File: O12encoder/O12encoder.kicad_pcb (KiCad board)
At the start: 2 copper layers, 14 x 14 mm, 15 parts, among them J1 Conn_01x06_Pin, J2 Conn_01x06_Pin, J3 Conn_01x06_Pin, J4 Conn_01x06_Pin, J5 SM02B-SRSS-TB_LF__SN_, J6 SM02B-SRSS-TB_LF__SN_, U1 QFN-3x3_MA702_MNP, U2 STM32L011F4Ux, U3 THVD1420DRLR

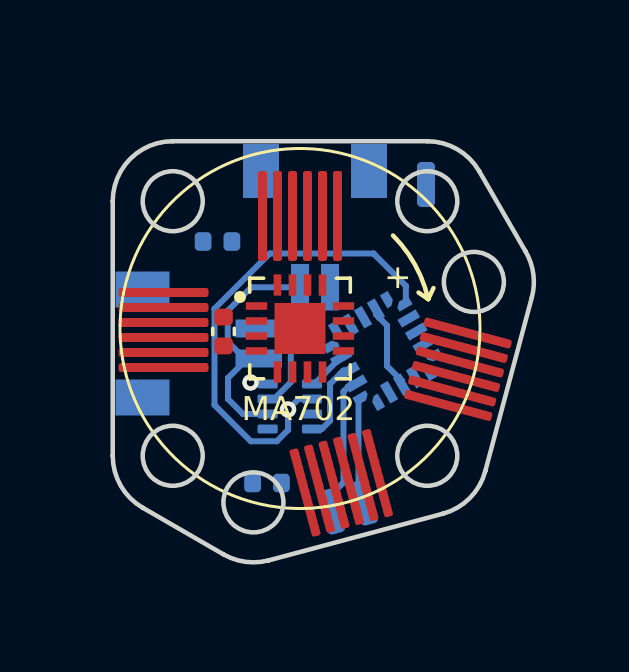
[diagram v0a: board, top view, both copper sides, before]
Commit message: encoder change to both sides FFC
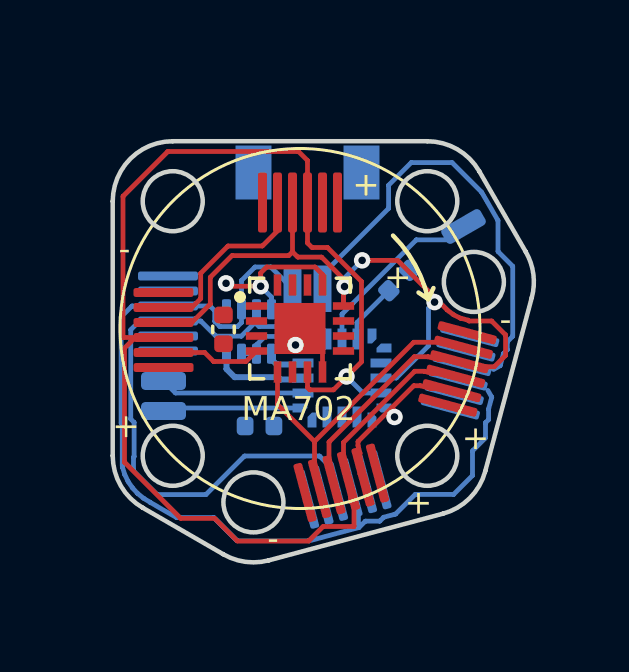
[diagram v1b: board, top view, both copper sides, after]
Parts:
- added J7: Conn_01x06_Pin, O32controller:FFC_0.5mm_6p, B.Cu at (55.7, 50.2)
- added J8: Conn_01x06_Pin, O32controller:FFC_0.5mm_6p, B.Cu at (50.3, 55.7)
- J5: value SM02B-SRSS-TB_LF__SN_ -> JST_SM02B-SRSS-TB(LF)(SN)
- J6: value SM02B-SRSS-TB_LF__SN_ -> Conn_01x06_Pin; footprint O32controller:JST_SM02B-SRSS-TB(LF)(SN) -> O32controller:FFC_0.5mm_6p
- U1: value QFN-3x3_MA702_MNP -> MA702GQ-P
- moved TP2 7.36 mm to (45.5, 52.8), turned to -90 degrees
- moved TP3 7.09 mm to (45.5, 51.8), turned to -90 degrees
- moved J6 6.39 mm to (45.6, 50.8)
- moved C3 6.19 mm to (53.3, 48.4), turned to 45 degrees
- moved J5 5.23 mm to (50.2, 46.7), turned to 0 degrees
- moved U3 2.85 mm to (48.3, 50.1), turned to 90 degrees
- moved J4 2.50 mm to (55.6, 50.1), turned to -15 degrees
- moved C2 1.92 mm to (48.6, 53.2)
- moved TP1 1.88 mm to (55.5, 46.6), turned to -60 degrees
- moved U2 1.62 mm to (51.4, 51.6), turned to -90 degrees
- moved J2 0.45 mm to (48.8, 45.8)
- moved C1 0.07 mm to (47.5, 50.0), turned to -90 degrees
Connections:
- net Net-(U2-NRST) renamed /NRST
- J6 pad 1: /RS485_A -> GND
- J6 pad 2: /RS485_B -> GND
- U1 pad 5: /~{MAG1_CS} -> /~{MAG2_CS}
- U2 pad 1: unconnected-(U2-PC14-Pad1) -> /UART_DE
- U2 pad 20: unconnected-(U2-PB9-Pad20) -> GND
- U2 pad 5: unconnected-(U2-PA0-Pad5) -> /ADC_IN0/WKUP
- U2 pad 6: /UART_DE -> unconnected-(U2-PA1-Pad6)
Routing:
- net /SPI_MISO: track 0.00 -> 46.0 mm, vias 0 -> 1
- net /SPI_SCLK: track 0.00 -> 29.2 mm, vias 0 -> 3
- net /RS485_B: track 7.08 -> 35.6 mm
- net /RS485_A: track 8.44 -> 30.8 mm
- net /~{MAG2_CS}: track 0.00 -> 15.3 mm
- net /UART_DE: track 16.0 -> 2.91 mm, vias 1 -> 0
- net /SPI_MOSI: track 0.00 -> 9.29 mm, vias 0 -> 1
- net /NRST: track 0.00 -> 6.04 mm
- net +3.3V: track 3.45 -> 7.15 mm, vias 1 -> 2
- net GND: track 0.00 -> 2.00 mm, vias 0 -> 1
- net /SWDIO: track 3.54 -> 4.52 mm
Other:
- board text added: "-"

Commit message: routed more, trouble with 3.3 and gnd
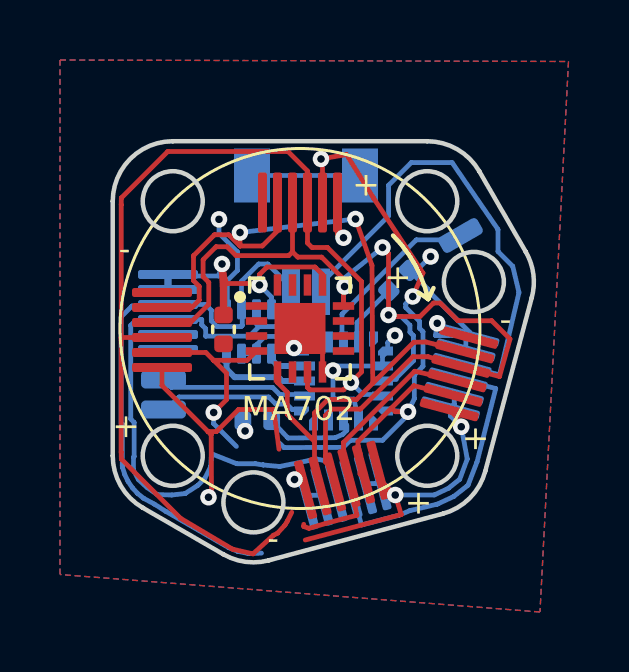
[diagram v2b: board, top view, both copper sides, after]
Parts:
- moved TP1 0.32 mm to (55.4, 46.9)
- moved C2 0.19 mm to (48.6, 53.1)
- moved J4 0.16 mm to (55.6, 50.3)
- moved U2 0.11 mm to (51.5, 51.8)
- moved J5 0.11 mm to (50.2, 46.8)
- moved J3 0.10 mm to (50.2, 55.4)
- moved J1 0.05 mm to (45.4, 48.8)
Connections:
- U2 pad 11: /SPI_MOSI -> unconnected-(U2-PB1-Pad11)
- U2 pad 6: unconnected-(U2-PA1-Pad6) -> GND
- U2 pad 7: unconnected-(U2-PA4-Pad7) -> GND
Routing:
- net +3.3V: track 7.15 -> 37.9 mm, vias 2 -> 6
- net /SPI_MOSI: track 9.29 -> 30.6 mm, vias 1 -> 4
- net GND: track 2.00 -> 18.9 mm, vias 1 -> 8
- net /~{MAG2_CS}: track 15.3 -> 27.4 mm, vias 0 -> 2
- net /SPI_SCLK: track 29.2 -> 32.9 mm
- net unconnected-(J5-Shield-PadS1): track 0.00 -> 3.60 mm
- net /RS485_B: track 35.6 -> 38.8 mm
- net /RS485_A: track 30.8 -> 29.2 mm
- net /SPI_MISO: track 46.0 -> 44.8 mm
- added copper zone on B.Cu, net GND
- added copper zone on F.Cu, net GND

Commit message: done? added silkscreen and pa0 breakout
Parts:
- removed J3: Conn_01x06_Pin, O32controller:FFC_0.5mm_6p
- added TP4: TestPoint, O32controller:TestPoint_Pad_Rect, B.Cu at (55.1, 47.0)
- TP1: moved to F.Cu
- moved C1 3.59 mm to (50.0, 52.5), turned to 0 degrees
- moved J6 2.50 mm to (45.6, 48.2), turned to 180 degrees
- moved J7 2.50 mm to (55.0, 52.6), turned to -15 degrees
- moved J8 2.50 mm to (52.7, 55.1), turned to 105 degrees
- moved J4 2.46 mm to (55.1, 52.7), turned to 165 degrees
- moved J2 0.50 mm to (48.8, 45.3)
- moved TP1 0.34 mm to (55.0, 47.1)
- moved J1 0.10 mm to (45.3, 48.8)
- moved C2 0.08 mm to (48.5, 53.1)
- turned U1 to 180 degrees
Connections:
- J5 pad S1: unconnected-(J5-Shield-PadS1) -> /RS485_A
- J5 pad S2: unconnected-(J5-Shield-PadS1) -> /RS485_A
- U2 pad 2: unconnected-(U2-PC15-Pad2) -> GND
- U2 pad 6: GND -> unconnected-(U2-PA1-Pad6)
- U2 pad 7: GND -> unconnected-(U2-PA4-Pad7)
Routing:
- net /SPI_MISO: track 44.8 -> 19.2 mm
- net /RS485_A: track 29.2 -> 50.9 mm, vias 0 -> 2
- net +3.3V: track 37.9 -> 50.7 mm, vias 6 -> 8
- net /~{MAG2_CS}: track 27.4 -> 18.6 mm
- net /ADC_IN0/WKUP: track 0.00 -> 8.72 mm
- net /SPI_SCLK: track 32.9 -> 38.0 mm
- net GND: track 18.9 -> 23.9 mm, vias 8 -> 10
- net unconnected-(J5-Shield-PadS1): track 3.60 -> 0.00 mm
- net /SPI_MOSI: track 30.6 -> 28.5 mm, vias 4 -> 3
- net /RS485_B: track 38.8 -> 37.4 mm
- net /NRST: track 6.04 -> 5.67 mm, vias 0 -> 1
- added copper zone on B.Cu, net +3.3V
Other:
- board text added: "+θ"
- board text added: "a"
- board text added: "b"
- board text added: "clk"
- board text added: "io"
- board text added: "pa0"
- board text added: "rs485"
- board text added: "rst"
- board text added: "spi"
- board text added: "Ø12encoder"
- board text removed: "MA702"
